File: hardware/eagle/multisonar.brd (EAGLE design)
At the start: 99 x 99 mm, 25 parts, among them IC1 ATMEGA328-20P, J1 ARDUINO_R3_SHIELD, Y1 16MHZ

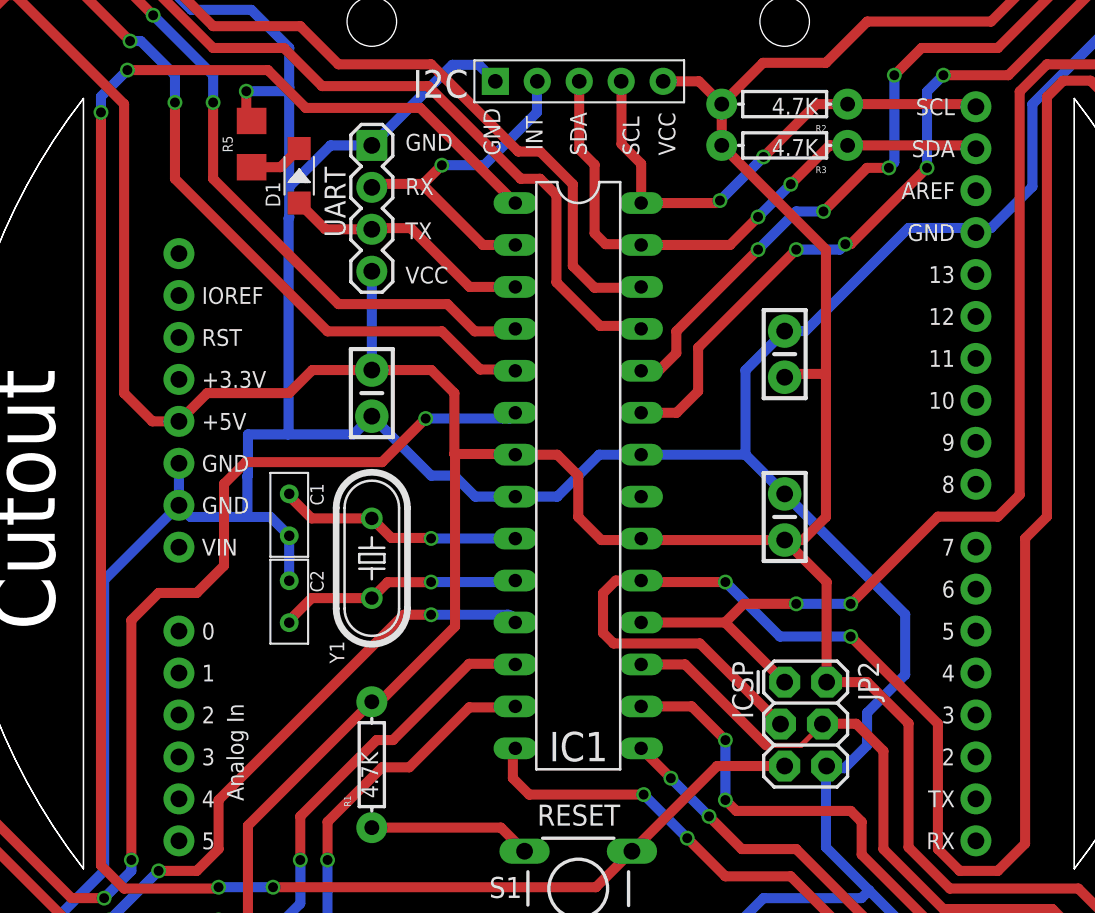
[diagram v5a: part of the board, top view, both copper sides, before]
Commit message: Use the lock package for easier soldering
The lock arduino shield package is used to facilitate
the headers staying in place while soldering
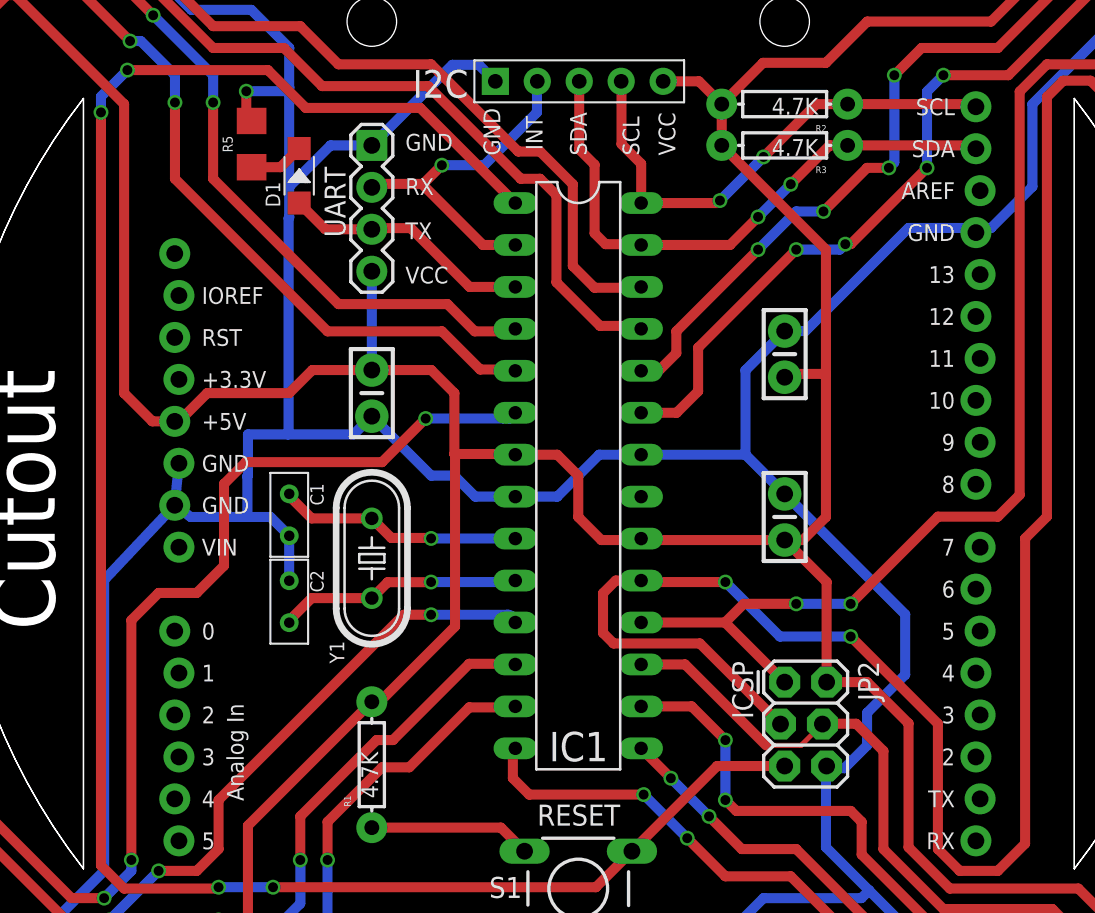
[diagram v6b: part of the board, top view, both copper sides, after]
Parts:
- J1: value ARDUINO_R3_SHIELD -> ARDUINO_R3_SHIELDUNO_R3_SHIELD_LOCK; device SparkFun-Boards:UNO_R3_SHIELD -> SparkFun-Boards:UNO_R3_SHIELD_LOCK
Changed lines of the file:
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@@
 <attribute name="PROD_ID" value="CAP-08370" x="95" y="57.36" size="1.778" layer="27" rot="R270" display="off"/>
 </element>
-<element name="J1" library="SparkFun-Boards" package="UNO_R3_SHIELD" value="ARDUINO_R3_SHIELD" x="109.1202" y="82.5" rot="R180"/>
+<element name="J1" library="SparkFun-Boards" package="UNO_R3_SHIELD_LOCK" value="ARDUINO_R3_SHIELDUNO_R3_SHIELD_LOCK" x="109.1202" y="82.5" rot="R180"/>
 <element name="JP2" library="SparkFun-Connectors" package="2X3_LOCK" value="ICSP" x="95" y="37.5" smashed="yes" rot="R270">
 <attribute name="NAME" x="99.445" y="38.77" size="1.27" layer="25" ratio="10" rot="R270"/>
@@
 <contactref element="UART" pad="4"/>
 <wire x1="97.5" y1="90" x2="105" y2="90" width="0.6096" layer="1"/>
-<wire x1="56.71" y1="53.29" x2="58.3202" y2="53.29" width="0.6096" layer="1"/>
-<wire x1="56.71" y1="53.29" x2="55" y2="55" width="0.6096" layer="1"/>
+<wire x1="55" y1="55" x2="56.71" y2="53.29" width="0.6096" layer="1"/>
 <wire x1="55" y1="55" x2="55" y2="72.5" width="0.6096" layer="1"/>
 <wire x1="55" y1="72.5" x2="48.398028125" y2="79.101971875" width="0.6096" layer="1"/>
@@
 <wire x1="96.103" y1="46.103" x2="97.5" y2="47.5" width="0.6096" layer="1"/>
 <wire x1="97.5" y1="63.69" x2="91.19" y2="70" width="0.6096" layer="1"/>
-<wire x1="58.3202" y1="53.29" x2="60.0302" y2="55" width="0.6096" layer="1"/>
 <wire x1="60.0302" y1="55" x2="65" y2="55" width="0.6096" layer="1"/>
 <wire x1="65" y1="55" x2="66.397" y2="56.397" width="0.6096" layer="1"/>
@@
 <wire x1="111.601975" y1="84.490125" x2="112.601975" y2="85.490125" width="0.6096" layer="1"/>
 <wire x1="47.9058" y1="79.101971875" x2="46.9058" y2="80.101971875" width="0.6096" layer="1"/>
+<wire x1="56.71" y1="53.29" x2="58.0662" y2="53.29" width="0.6096" layer="1"/>
+<wire x1="58.0662" y1="53.29" x2="58.3202" y2="53.29" width="0.6096" layer="1"/>
+<wire x1="58.3202" y1="53.29" x2="60.0302" y2="55" width="0.6096" layer="1"/>
 </signal>
 <signal name="GND">
@@
 <wire x1="106.5802" y1="64.72" x2="106.8602" y2="65" width="0.6096" layer="16"/>
 <wire x1="110" y1="67.5" x2="110" y2="72.5" width="0.6096" layer="16"/>
-<wire x1="58.3202" y1="48.21" x2="58.3202" y2="50.75" width="0.6096" layer="16"/>
-<wire x1="58.3202" y1="48.21" x2="59.0302" y2="47.5" width="0.6096" layer="16"/>
+<wire x1="58.0662" y1="48.21" x2="58.3202" y2="50.75" width="0.6096" layer="16"/>
+<wire x1="58.0662" y1="48.21" x2="59.0302" y2="47.5" width="0.6096" layer="16"/>
 <wire x1="59.0302" y1="47.5" x2="62.46360625" y2="47.5" width="0.6096" layer="16"/>
 <wire x1="68.897" y1="52.5" x2="70" y2="53.603" width="0.6096" layer="16"/>
@@
 <wire x1="53.79" y1="26.07" x2="48.513946875" y2="20.793946875" width="0.6096" layer="16"/>
 <wire x1="53.79" y1="26.07" x2="53.79" y2="43.6798" width="0.6096" layer="16"/>
-<wire x1="53.79" y1="43.6798" x2="58.3202" y2="48.21" width="0.6096" layer="16"/>
+<wire x1="53.79" y1="43.6798" x2="58.0662" y2="48.21" width="0.6096" layer="16"/>
 <wire x1="85.7512" y1="22.7394" x2="92.0394" y2="22.7394" width="0.6096" layer="16"/>
 <wire x1="92.0394" y1="22.7394" x2="93.72" y2="24.42" width="0.6096" layer="16"/>
@@
 <contactref element="R3" pad="P$1"/>
 <contactref element="J1" pad="SDA"/>
-<wire x1="106.5802" y1="69.8" x2="106.3802" y2="70" width="0.6096" layer="1"/>
-<wire x1="98.81" y1="70" x2="106.3802" y2="70" width="0.6096" layer="1"/>
 <wire x1="86.31" y1="63.97" x2="91.69" y2="63.97" width="0.6096" layer="1"/>
 <wire x1="91.69" y1="63.97" x2="93.39" y2="65.67" width="0.6096" layer="1"/>
@@
 <wire x1="83.49" y1="64.68" x2="83.49" y2="68.83" width="0.6096" layer="1"/>
 <wire x1="82.56" y1="69.76" x2="82.56" y2="73.88" width="0.6096" layer="1"/>
+<wire x1="98.81" y1="70" x2="106.3802" y2="70" width="0.6096" layer="1"/>
+<wire x1="106.3802" y1="70" x2="106.5802" y2="69.8" width="0.6096" layer="1"/>
 </signal>
 <signal name="SCL">
@@
 <contactref element="IC1" pad="28"/>
 <contactref element="J1" pad="SCL"/>
-<wire x1="106.5802" y1="72.34" x2="106.4202" y2="72.5" width="0.6096" layer="1"/>
-<wire x1="98.81" y1="72.5" x2="106.4202" y2="72.5" width="0.6096" layer="1"/>
 <wire x1="90.93" y1="66.51" x2="86.31" y2="66.51" width="0.6096" layer="1"/>
 <wire x1="90.93" y1="66.51" x2="91.08" y2="66.66" width="0.6096" layer="1"/>
@@
 <wire x1="85.12" y1="70.08" x2="85.12" y2="73.86" width="0.6096" layer="1"/>
 <wire x1="85.12" y1="73.86" x2="85.1" y2="73.88" width="0.6096" layer="1"/>
+<wire x1="98.81" y1="72.5" x2="106.4202" y2="72.5" width="0.6096" layer="1"/>
+<wire x1="106.4202" y1="72.5" x2="106.5802" y2="72.34" width="0.6096" layer="1"/>
 </signal>
 <signal name="RST">

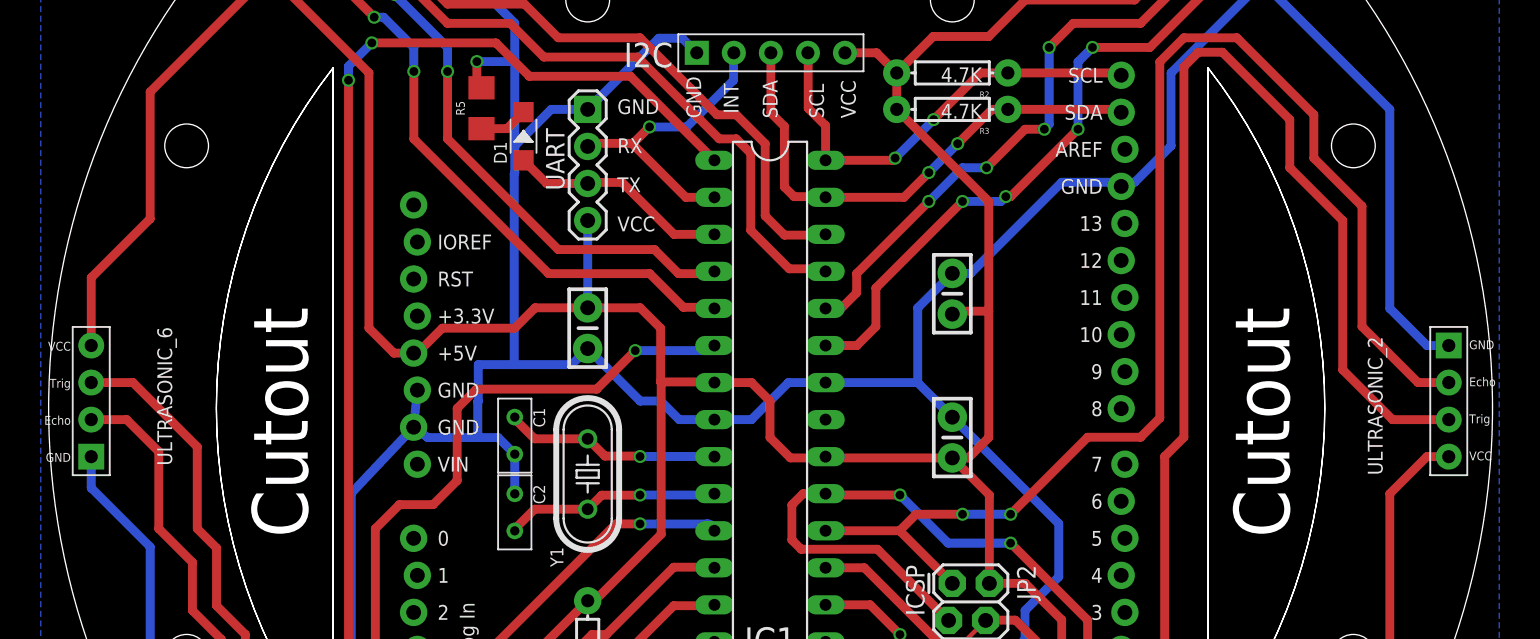
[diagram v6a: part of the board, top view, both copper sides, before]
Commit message: Ultrasonic position fix
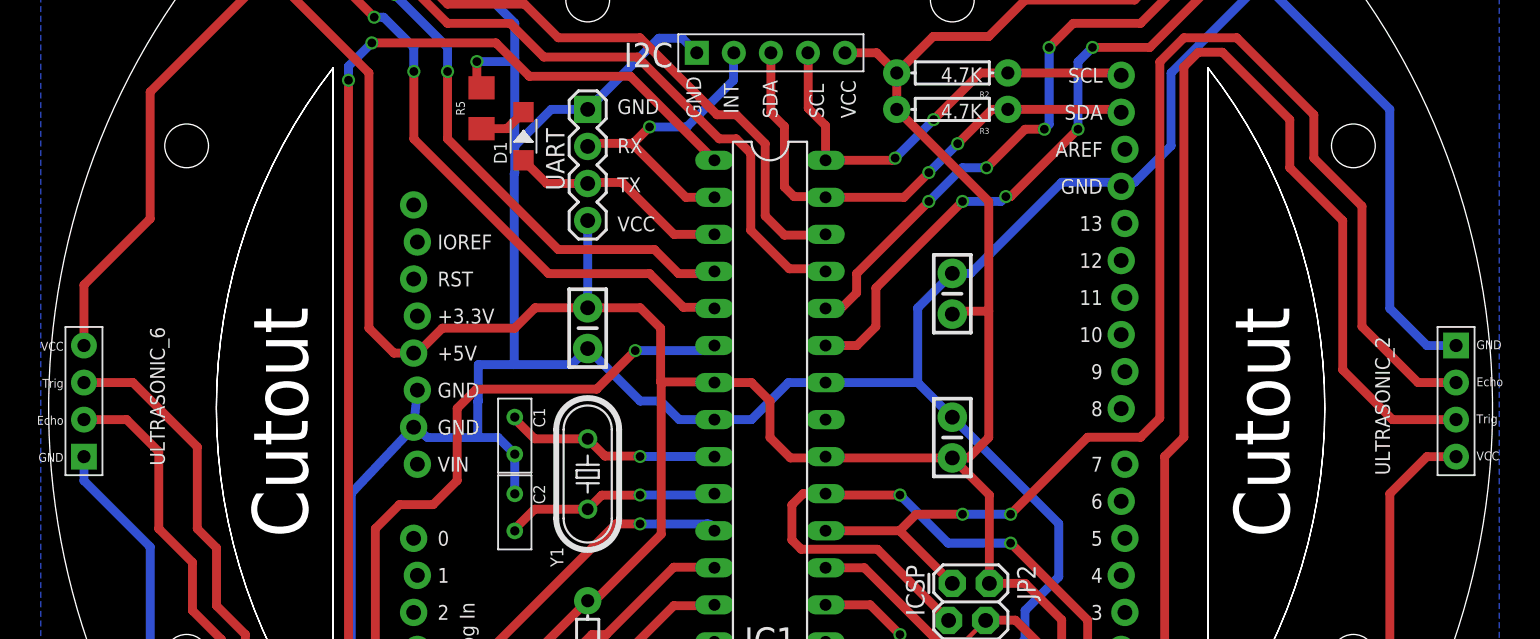
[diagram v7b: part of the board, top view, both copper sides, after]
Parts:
- moved ULTRASONIC_2 0.50 mm to (127.0, 50.0)
- moved ULTRASONIC_6 0.50 mm to (38.0, 50.0)
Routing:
- net VCC: track 365.7 -> 366.4 mm
- net GND: track 390.4 -> 391.1 mm
- net PD5: track 70.3 -> 70.8 mm
- net PD4: track 85.9 -> 86.4 mm
- net PB5: track 136.4 -> 136.9 mm
- net PB4: track 92.5 -> 93.0 mm
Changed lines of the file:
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@@
 <element name="ULTRASONIC_0" library="Ultrasonic Sensor HC-SR04" package="HC-SR04_FOOTPRINT" value="HC-SR04" x="82.5" y="94" rot="R90"/>
 <element name="ULTRASONIC_1" library="Ultrasonic Sensor HC-SR04" package="HC-SR04_FOOTPRINT" value="HC-SR04" x="113.5" y="81" rot="MR135"/>
-<element name="ULTRASONIC_2" library="Ultrasonic Sensor HC-SR04" package="HC-SR04_FOOTPRINT" value="HC-SR04" x="126.5" y="50"/>
+<element name="ULTRASONIC_2" library="Ultrasonic Sensor HC-SR04" package="HC-SR04_FOOTPRINT" value="HC-SR04" x="127" y="50"/>
 <element name="ULTRASONIC_7" library="Ultrasonic Sensor HC-SR04" package="HC-SR04_FOOTPRINT" value="HC-SR04" x="51.395925" y="81" rot="MR45"/>
 <element name="ULTRASONIC_4" library="Ultrasonic Sensor HC-SR04" package="HC-SR04_FOOTPRINT" value="HC-SR04" x="82.5" y="5.12" rot="R270"/>
 <element name="ULTRASONIC_5" library="Ultrasonic Sensor HC-SR04" package="HC-SR04_FOOTPRINT" value="HC-SR04" x="50.895925" y="18.395921875" rot="MR315"/>
-<element name="ULTRASONIC_6" library="Ultrasonic Sensor HC-SR04" package="HC-SR04_FOOTPRINT" value="HC-SR04" x="38.5" y="50" rot="R180"/>
+<element name="ULTRASONIC_6" library="Ultrasonic Sensor HC-SR04" package="HC-SR04_FOOTPRINT" value="HC-SR04" x="38" y="50" rot="R180"/>
 <element name="ULTRASONIC_3" library="Ultrasonic Sensor HC-SR04" package="HC-SR04_FOOTPRINT" value="HC-SR04" x="114" y="18.395921875" rot="MR225"/>
 <element name="IC1" library="atmega328" package="DIL28-3" value="ATMEGA328-20P" x="82.5" y="50" smashed="yes" rot="R270">
@@
 <wire x1="74.92" y1="2.58" x2="65" y2="12.5" width="0.6096" layer="1"/>
 <wire x1="125" y1="43.65" x2="127.54" y2="46.19" width="0.6096" layer="1"/>
-<wire x1="127.54" y1="46.19" x2="129.04" y2="46.19" width="0.6096" layer="1"/>
-<wire x1="35.96" y1="58.46" x2="35.96" y2="53.81" width="0.6096" layer="1"/>
-<wire x1="35.96" y1="58.46" x2="40" y2="62.5" width="0.6096" layer="1"/>
+<wire x1="127.54" y1="46.19" x2="129.54" y2="46.19" width="0.6096" layer="1"/>
 <wire x1="116.3704125" y1="21.4136625" x2="118.490128125" y2="19.293946875" width="0.6096" layer="1"/>
 <wire x1="51.793953125" y1="13.90579375" x2="51.793953125" y2="14.293953125" width="0.6096" layer="1"/>
@@
 <wire x1="105" y1="90" x2="110.509875" y2="84.490125" width="0.6096" layer="1"/>
 <wire x1="40" y1="71.196171875" x2="47.9058" y2="79.101971875" width="0.6096" layer="1"/>
-<wire x1="40" y1="62.5" x2="40" y2="71.196171875" width="0.6096" layer="1"/>
+<wire x1="40" y1="71.196171875" x2="40" y2="62.5" width="0.6096" layer="1"/>
 <wire x1="87.64" y1="73.88" x2="89.81" y2="73.88" width="0.6096" layer="1"/>
 <wire x1="89.81" y1="73.88" x2="91.19" y2="72.5" width="0.6096" layer="1"/>
@@
 <wire x1="58.0662" y1="53.29" x2="58.3202" y2="53.29" width="0.6096" layer="1"/>
 <wire x1="58.3202" y1="53.29" x2="60.0302" y2="55" width="0.6096" layer="1"/>
+<wire x1="35.46" y1="57.96" x2="35.46" y2="53.81" width="0.6096" layer="1"/>
+<wire x1="40" y1="62.5" x2="35.46" y2="57.96" width="0.6096" layer="1"/>
 </signal>
 <signal name="GND">
@@
 <wire x1="101.40579375" y1="13.90579375" x2="90.08" y2="2.58" width="0.6096" layer="16"/>
 <wire x1="125" y1="56.35" x2="127.54" y2="53.81" width="0.6096" layer="16"/>
-<wire x1="127.54" y1="53.81" x2="129.04" y2="53.81" width="0.6096" layer="16"/>
-<wire x1="35.96" y1="44.04" x2="35.96" y2="46.19" width="0.6096" layer="16"/>
-<wire x1="40" y1="40" x2="35.96" y2="44.04" width="0.6096" layer="16"/>
+<wire x1="127.54" y1="53.81" x2="129.54" y2="53.81" width="0.6096" layer="16"/>
 <wire x1="113.101975" y1="14.398025" x2="113.101975" y2="13.90579375" width="0.6096" layer="16"/>
 <wire x1="105" y1="22.5" x2="113.101975" y2="14.398025" width="0.6096" layer="16"/>
@@
 <wire x1="52.293953125" y1="85.490125" x2="52.293953125" y2="86.461309375" width="0.6096" layer="16"/>
 <wire x1="52.293953125" y1="86.461309375" x2="52.83264375" y2="87" width="0.6096" layer="16"/>
+<wire x1="35.46" y1="44.54" x2="35.46" y2="46.19" width="0.6096" layer="16"/>
+<wire x1="40" y1="40" x2="35.46" y2="44.54" width="0.6096" layer="16"/>
 </signal>
 <signal name="N$3">
@@
 <wire x1="59.4" y1="42.9" x2="61.05" y2="44.55" width="0.6096" layer="1"/>
 <wire x1="62.37" y1="50.82" x2="70.62" y2="50.82" width="0.6096" layer="1"/>
-<wire x1="38.82" y1="51.27" x2="35.96" y2="51.27" width="0.6096" layer="1"/>
+<wire x1="38.82" y1="51.27" x2="35.46" y2="51.27" width="0.6096" layer="1"/>
 </signal>
 <signal name="PD5">
@@
 <wire x1="57.09" y1="26.07" x2="59.4" y2="26.07" width="0.6096" layer="1"/>
 <wire x1="54.12" y1="23.1" x2="57.09" y2="26.07" width="0.6096" layer="16"/>
-<wire x1="38.39" y1="48.73" x2="35.96" y2="48.73" width="0.6096" layer="1"/>
+<wire x1="38.39" y1="48.73" x2="35.46" y2="48.73" width="0.6096" layer="1"/>
 </signal>
 <signal name="PD6">
@@
 <wire x1="104.28" y1="47.52" x2="99" y2="42.24" width="0.6096" layer="1"/>
 <wire x1="109.23" y1="73.26" x2="109.23" y2="48.84" width="0.6096" layer="1"/>
-<wire x1="126.93" y1="51.27" x2="129.04" y2="51.27" width="0.6096" layer="1"/>
+<wire x1="126.93" y1="51.27" x2="129.54" y2="51.27" width="0.6096" layer="1"/>
 </signal>
 <signal name="PB5">
@@
 <wire x1="110.88" y1="47.52" x2="109.56" y2="46.2" width="0.6096" layer="1"/>
 <wire x1="111.87" y1="73.92" x2="110.88" y2="72.93" width="0.6096" layer="1"/>
-<wire x1="125.18" y1="48.73" x2="129.04" y2="48.73" width="0.6096" layer="1"/>
+<wire x1="125.18" y1="48.73" x2="129.54" y2="48.73" width="0.6096" layer="1"/>
 </signal>
 <signal name="RX/INT">
